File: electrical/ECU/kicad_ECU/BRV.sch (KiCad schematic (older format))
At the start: 5 parts

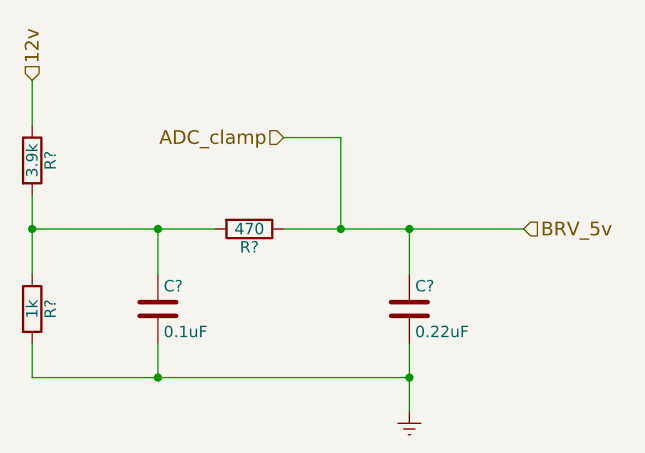
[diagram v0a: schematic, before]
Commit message: fixed some naming errors and initial round of double checking
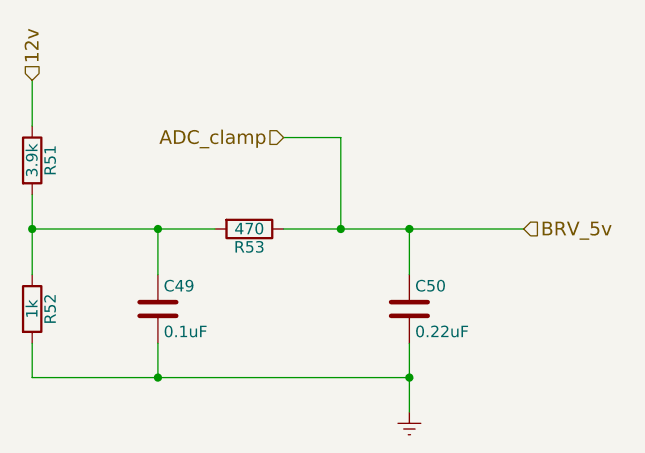
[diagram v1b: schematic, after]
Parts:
- gave numbers to parts that had none: 5
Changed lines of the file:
@@
 $Descr A4 11693 8268
 encoding utf-8
-Sheet 19 33
+Sheet 23 33
 Title "Battery Refernece Voltage"
 Date ""
@@
 12v
 $Comp
-L R R?
+L R R51
 U 1 1 59783EC3
 P 5000 3250
-F 0 "R?" V 5080 3250 50  0000 C CNN
+F 0 "R51" V 5080 3250 50  0000 C CNN
 F 1 "3.9k" V 5000 3250 50  0000 C CNN
 F 2 "" V 4930 3250 50  0001 C CNN
@@
 $EndComp
 $Comp
-L R R?
+L R R52
 U 1 1 59783EE2
 P 5000 3900
-F 0 "R?" V 5080 3900 50  0000 C CNN
+F 0 "R52" V 5080 3900 50  0000 C CNN
 F 1 "1k" V 5000 3900 50  0000 C CNN
 F 2 "" V 4930 3900 50  0001 C CNN
@@
 $EndComp
 $Comp
-L C C?
+L C C49
 U 1 1 59783F06
 P 5550 3900
-F 0 "C?" H 5575 4000 50  0000 L CNN
+F 0 "C49" H 5575 4000 50  0000 L CNN
 F 1 "0.1uF" H 5575 3800 50  0000 L CNN
 F 2 "" H 5588 3750 50  0001 C CNN
@@
 $EndComp
 $Comp
-L C C?
+L C C50
 U 1 1 59783F32
 P 6650 3900
-F 0 "C?" H 6675 4000 50  0000 L CNN
+F 0 "C50" H 6675 4000 50  0000 L CNN
 F 1 "0.22uF" H 6675 3800 50  0000 L CNN
 F 2 "" H 6688 3750 50  0001 C CNN
@@
 $EndComp
 $Comp
-L R R?
+L R R53
 U 1 1 59783F66
 P 5950 3550
-F 0 "R?" V 6030 3550 50  0000 C CNN
+F 0 "R53" V 6030 3550 50  0000 C CNN
 F 1 "470" V 5950 3550 50  0000 C CNN
 F 2 "" V 5880 3550 50  0001 C CNN
@@
 Connection ~ 6650 3550
 $Comp
-L Earth #PWR?
+L Earth #PWR52
 U 1 1 59784002
 P 6650 4350
-F 0 "#PWR?" H 6650 4100 50  0001 C CNN
+F 0 "#PWR52" H 6650 4100 50  0001 C CNN
 F 1 "Earth" H 6650 4200 50  0001 C CNN
 F 2 "" H 6650 4350 50  0001 C CNN
